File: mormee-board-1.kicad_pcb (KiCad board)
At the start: 4 copper layers, 40 x 60 mm, 167 parts, among them J2 24FLZ-SM2-TB, J3 USB4105-GF-A, J4 S2B-PH-SM4-TB(LF)(SN), J5 DM3BT-DSF-PEJS, M1 IMP34DT05TR, M2 IMP34DT05TR, Q1 AO3401A, SW1 EVQ-PUB02K, SW2 EVQ-PUB02K, U1 W25Q128JVSIQ, U10 MAX17048G+T10, U11 MP2637GR-P, U2 RTL8735BDM-A20-N04, U3 FDS9926A, U4 FT232RNL-REEL, U5 RT8097AHGE, U6 RT8097AHGE, U7 RT9080-28GJ5, U8 RT9080-18GJ5, U9 RT9080-12GJ5

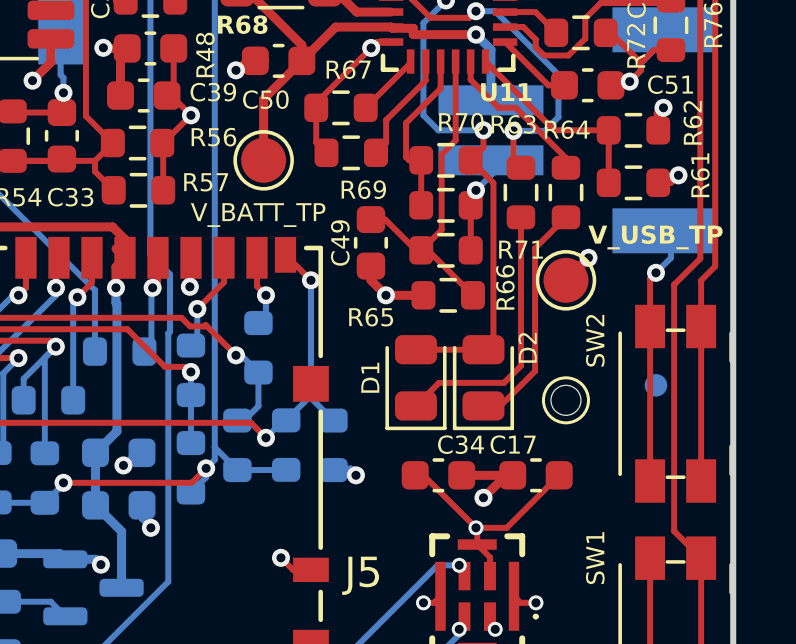
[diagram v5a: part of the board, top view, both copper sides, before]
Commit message: Updated LED footprint to 0603, which was easier to find
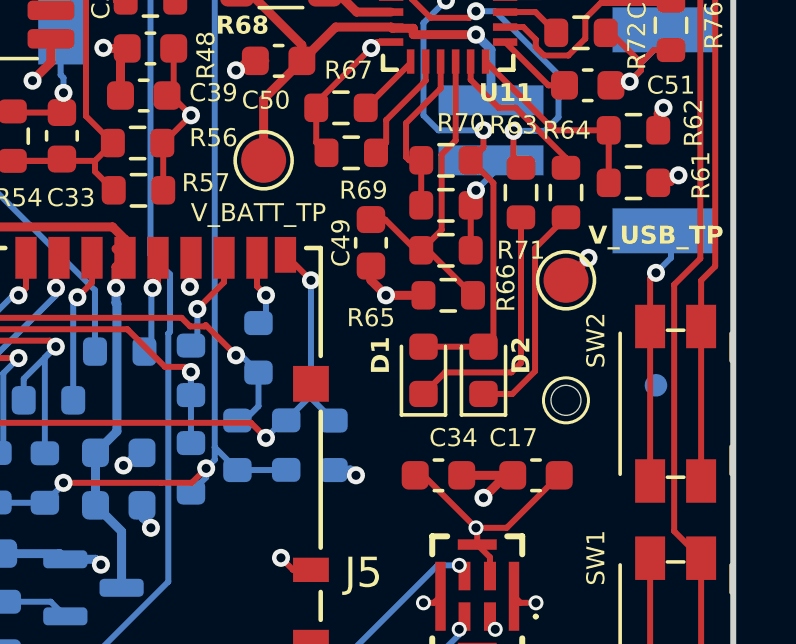
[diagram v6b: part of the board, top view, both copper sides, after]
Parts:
- C51, C53: value 100nF_10V -> 0.1uF_10V
- D1: value LED_2012_RED -> RED LED; footprint LED_SMD:LED_0805_2012Metric -> LED_SMD:LED_0603_1608Metric
- D2: value LED_2012_BLUE -> BLUE LED; footprint LED_SMD:LED_0805_2012Metric -> LED_SMD:LED_0603_1608Metric
- moved D1 0.35 mm to (99.0, 88.0)
- moved D2 0.25 mm to (101.0, 88.0)
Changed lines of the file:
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@@
 		)
 	)
-	(footprint "LED_SMD:LED_0805_2012Metric"
+	(footprint "LED_SMD:LED_0603_1608Metric"
 		(layer "F.Cu")
-		(at 101 88.25 90)
-		(descr "LED SMD 0805 (2012 Metric), square (rectangular) end terminal, IPC-7351 nominal, (Body size source: https://docs.google.com/spreadsheets/d/1BsfQQcO9C6DZCsRaXUlFlo91Tg2WpOkGARC1WS5S8t0/edit?usp=sharing), generated with kicad-footprint-generator")
+		(at 101 88 90)
+		(descr "LED SMD 0603 (1608 Metric), square (rectangular) end terminal, IPC-7351 nominal, (Body size source: http://www.tortai-tech.com/upload/download/2011102023233369053.pdf), generated with kicad-footprint-generator")
 		(tags "LED")
 		(property "Reference" "D2"
-			(at 1 1.5 90)
+			(at 0.5 1.25 90)
 			(layer "F.SilkS")
 			(effects
@@
 					(size 0.6 0.6)
 					(thickness 0.1)
+					(bold yes)
 				)
 			)
 		)
-		(property "Value" "LED_2012_BLUE"
-			(at 0 1.65 90)
+		(property "Value" "BLUE LED"
+			(at 0 1.43 90)
 			(layer "F.Fab")
 			(effects
@@
 		(attr smd)
 		(fp_line
-			(start 1 -0.96)
-			(end -1.685 -0.96)
+			(start 0.8 -0.735)
+			(end -1.485 -0.735)
 			(stroke
 				(width 0.12)
@@
 		)
 		(fp_line
-			(start -1.685 -0.96)
-			(end -1.685 0.96)
+			(start -1.485 -0.735)
+			(end -1.485 0.735)
 			(stroke
 				(width 0.12)
@@
 		)
 		(fp_line
-			(start -1.685 0.96)
-			(end 1 0.96)
+			(start -1.485 0.735)
+			(end 0.8 0.735)
 			(stroke
 				(width 0.12)
@@
 		)
 		(fp_rect
-			(start -1.68 -0.95)
-			(end 1.68 0.95)
+			(start -1.48 -0.73)
+			(end 1.48 0.73)
 			(stroke
 				(width 0.05)
@@
 		)
 		(fp_line
-			(start 1 -0.6)
-			(end -0.7 -0.6)
+			(start 0.8 -0.4)
+			(end -0.5 -0.4)
 			(stroke
 				(width 0.1)
@@
 		)
 		(fp_line
-			(start -0.7 -0.6)
-			(end -1 -0.3)
+			(start -0.5 -0.4)
+			(end -0.8 -0.1)
 			(stroke
 				(width 0.1)
@@
 		)
 		(fp_line
-			(start -1 -0.3)
-			(end -1 0.6)
+			(start -0.8 -0.1)
+			(end -0.8 0.4)
 			(stroke
 				(width 0.1)
@@
 		)
 		(fp_line
-			(start 1 0.6)
-			(end 1 -0.6)
+			(start 0.8 0.4)
+			(end 0.8 -0.4)
 			(stroke
 				(width 0.1)
@@
 		)
 		(fp_line
-			(start -1 0.6)
-			(end 1 0.6)
+			(start -0.8 0.4)
+			(end 0.8 0.4)
 			(stroke
 				(width 0.1)
@@
 		)
 		(fp_text user "${REFERENCE}"
-			(at 2.4375 0 90)
+			(at 0 0 90)
 			(layer "F.Fab")
 			(effects
 				(font
-					(size 0.6 0.6)
-					(thickness 0.1)
+					(size 0.4 0.4)
+					(thickness 0.06)
 				)
 			)
 		)
 		(pad "1" smd roundrect
-			(at -0.9375 0 90)
-			(size 0.975 1.4)
+			(at -0.7875 0 90)
+			(size 0.875 0.95)
 			(layers "F.Cu" "F.Mask" "F.Paste")
 			(roundrect_rratio 0.25)
@@
 		)
 		(pad "2" smd roundrect
-			(at 0.9375 0 90)
-			(size 0.975 1.4)
+			(at 0.7875 0 90)
+			(size 0.875 0.95)
 			(layers "F.Cu" "F.Mask" "F.Paste")
 			(roundrect_rratio 0.25)
@@
 		)
 		(embedded_fonts no)
-		(model "${KICAD9_3DMODEL_DIR}/LED_SMD.3dshapes/LED_0805_2012Metric.step"
+		(model "${KICAD9_3DMODEL_DIR}/LED_SMD.3dshapes/LED_0603_1608Metric.step"
 			(offset
 				(xyz 0 0 0)
@@
 			)
 		)
-		(property "Value" "100nF_10V"
+		(property "Value" "0.1uF_10V"
 			(at 0 1.43 0)
 			(layer "F.Fab")
@@
 		)
 	)
-	(footprint "LED_SMD:LED_0805_2012Metric"
+	(footprint "LED_SMD:LED_0603_1608Metric"
 		(layer "F.Cu")
-		(at 98.75 88.25 90)
-		(descr "LED SMD 0805 (2012 Metric), square (rectangular) end terminal, IPC-7351 nominal, (Body size source: https://docs.google.com/spreadsheets/d/1BsfQQcO9C6DZCsRaXUlFlo91Tg2WpOkGARC1WS5S8t0/edit?usp=sharing), generated with kicad-footprint-generator")
+		(at 99 88 90)
+		(descr "LED SMD 0603 (1608 Metric), square (rectangular) end terminal, IPC-7351 nominal, (Body size source: http://www.tortai-tech.com/upload/download/2011102023233369053.pdf), generated with kicad-footprint-generator")
 		(tags "LED")
 		(property "Reference" "D1"
-			(at 0 -1.5 90)
+			(at 0.5 -1.43 90)
 			(layer "F.SilkS")
 			(effects
@@
 					(size 0.6 0.6)
 					(thickness 0.1)
+					(bold yes)
 				)
 			)
 		)
-		(property "Value" "LED_2012_RED"
-			(at 0 1.65 90)
+		(property "Value" "RED LED"
+			(at 0 1.43 90)
 			(layer "F.Fab")
 			(effects
@@
 		(attr smd)
 		(fp_line
-			(start 1 -0.96)
-			(end -1.685 -0.96)
+			(start 0.8 -0.735)
+			(end -1.485 -0.735)
 			(stroke
 				(width 0.12)
@@
 		)
 		(fp_line
-			(start -1.685 -0.96)
-			(end -1.685 0.96)
+			(start -1.485 -0.735)
+			(end -1.485 0.735)
 			(stroke
 				(width 0.12)
@@
 		)
 		(fp_line
-			(start -1.685 0.96)
-			(end 1 0.96)
+			(start -1.485 0.735)
+			(end 0.8 0.735)
 			(stroke
 				(width 0.12)
@@
 		)
 		(fp_rect
-			(start -1.68 -0.95)
-			(end 1.68 0.95)
+			(start -1.48 -0.73)
+			(end 1.48 0.73)
 			(stroke
 				(width 0.05)
@@
 		)
 		(fp_line
-			(start 1 -0.6)
-			(end -0.7 -0.6)
+			(start 0.8 -0.4)
+			(end -0.5 -0.4)
 			(stroke
 				(width 0.1)
@@
 		)
 		(fp_line
-			(start -0.7 -0.6)
-			(end -1 -0.3)
+			(start -0.5 -0.4)
+			(end -0.8 -0.1)
 			(stroke
 				(width 0.1)
@@
 		)
 		(fp_line
-			(start -1 -0.3)
-			(end -1 0.6)
+			(start -0.8 -0.1)
+			(end -0.8 0.4)
 			(stroke
 				(width 0.1)
@@
 		)
 		(fp_line
-			(start 1 0.6)
-			(end 1 -0.6)
+			(start 0.8 0.4)
+			(end 0.8 -0.4)
 			(stroke
 				(width 0.1)
@@
 		)
 		(fp_line
-			(start -1 0.6)
-			(end 1 0.6)
+			(start -0.8 0.4)
+			(end 0.8 0.4)
 			(stroke
 				(width 0.1)
@@
 		)
 		(fp_text user "${REFERENCE}"
-			(at 2.6775 0.105 90)
+			(at 0 0 90)
 			(layer "F.Fab")
 			(effects
 				(font
-					(size 0.6 0.6)
-					(thickness 0.1)
+					(size 0.4 0.4)
+					(thickness 0.06)
 				)
 			)
 		)
 		(pad "1" smd roundrect
-			(at -0.9375 0 90)
-			(size 0.975 1.4)
+			(at -0.7875 0 90)
+			(size 0.875 0.95)
 			(layers "F.Cu" "F.Mask" "F.Paste")
 			(roundrect_rratio 0.25)
@@
 		)
 		(pad "2" smd roundrect
-			(at 0.9375 0 90)
-			(size 0.975 1.4)
+			(at 0.7875 0 90)
+			(size 0.875 0.95)
 			(layers "F.Cu" "F.Mask" "F.Paste")
 			(roundrect_rratio 0.25)
@@
 		)
 		(embedded_fonts no)
-		(model "${KICAD9_3DMODEL_DIR}/LED_SMD.3dshapes/LED_0805_2012Metric.step"
+		(model "${KICAD9_3DMODEL_DIR}/LED_SMD.3dshapes/LED_0603_1608Metric.step"
 			(offset
 				(xyz 0 0 0)
@@
 		(tags "resistor")
 		(property "Reference" "R63"
-			(at 2.25 -0.25 -0)
+			(at 2.25 -0.25 0)
 			(layer "F.SilkS")
 			(effects
@@
 			)
 		)
-		(property "Value" "100nF_10V"
+		(property "Value" "0.1uF_10V"
 			(at 0 1.43 0)
 			(layer "F.Fab")
@@
 		(tags "capacitor")
 		(property "Reference" "C17"
-			(at 0.75 1 0)
+			(at 0.75 1.25 0)
 			(layer "F.SilkS")
 			(effects
@@
 		(tags "capacitor")
 		(property "Reference" "C34"
-			(at -0.75 1 0)
+			(at -0.5 1.25 0)
 			(layer "F.SilkS")
 			(effects
@@
 	)
 	(segment
-		(start 101 87.3125)
-		(end 98.75 87.3125)
-		(width 0.2)
-		(layer "F.Cu")
-		(net 27)
-	)
-	(segment
 		(start 105.075 72.182835)
 		(end 104.445448 71.553283)
@@
 	)
 	(segment
-		(start 101.331 81.756)
-		(end 101.331 86.9815)
+		(start 101.307794 75.557794)
+		(end 101.199003 75.449003)
 		(width 0.2)
 		(layer "F.Cu")
@@
 	)
 	(segment
-		(start 101.307794 75.557794)
-		(end 101.199003 75.449003)
+		(start 101.331 81.756)
+		(end 101.331 86.8815)
 		(width 0.2)
 		(layer "F.Cu")
@@
 	)
 	(segment
-		(start 101.331 86.9815)
-		(end 101 87.3125)
+		(start 101.331 86.8815)
+		(end 101 87.2125)
+		(width 0.2)
+		(layer "F.Cu")
+		(net 27)
+	)
+	(segment
+		(start 101 87.2125)
+		(end 99 87.2125)
 		(width 0.2)
 		(layer "F.Cu")
@@
 	(segment
 		(start 102.25 82.9)
-		(end 102.25 87.849362)
+		(end 102.25 87.75)
 		(width 0.2)
 		(layer "F.Cu")
@@
 	)
 	(segment
-		(start 101.680362 88.419)
-		(end 99.5185 88.419)
+		(start 102.25 87.75)
+		(end 101.931 88.069)
 		(width 0.2)
 		(layer "F.Cu")
@@
 	)
 	(segment
-		(start 102.25 87.849362)
-		(end 101.680362 88.419)
+		(start 99.7185 88.069)
+		(end 99 88.7875)
 		(width 0.2)
 		(layer "F.Cu")
@@
 	)
 	(segment
-		(start 99.5185 88.419)
-		(end 98.75 89.1875)
+		(start 101.931 88.069)
+		(end 99.7185 88.069)
 		(width 0.2)
 		(layer "F.Cu")
@@
 	)
 	(segment
-		(start 101.5625 89.1875)
-		(end 101 89.1875)
+		(start 101.9625 88.7875)
+		(end 101 88.7875)
 		(width 0.2)
 		(layer "F.Cu")
@@
 	)
 	(segment
-		(start 103.75 82.9)
-		(end 102.719 83.931)
+		(start 102.719 88.031)
+		(end 101.9625 88.7875)
 		(width 0.2)
 		(layer "F.Cu")
@@
 	)
 	(segment
-		(start 102.719 88.031)
-		(end 101.5625 89.1875)
+		(start 103.75 82.9)
+		(end 102.719 83.931)
 		(width 0.2)
 		(layer "F.Cu")

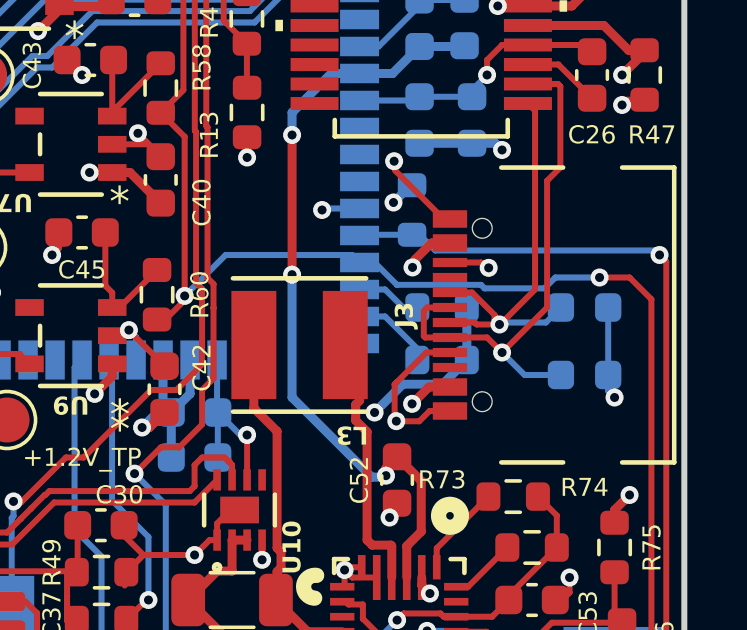
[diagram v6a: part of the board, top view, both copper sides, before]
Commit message: Updated USB connector pads to be manufacturable
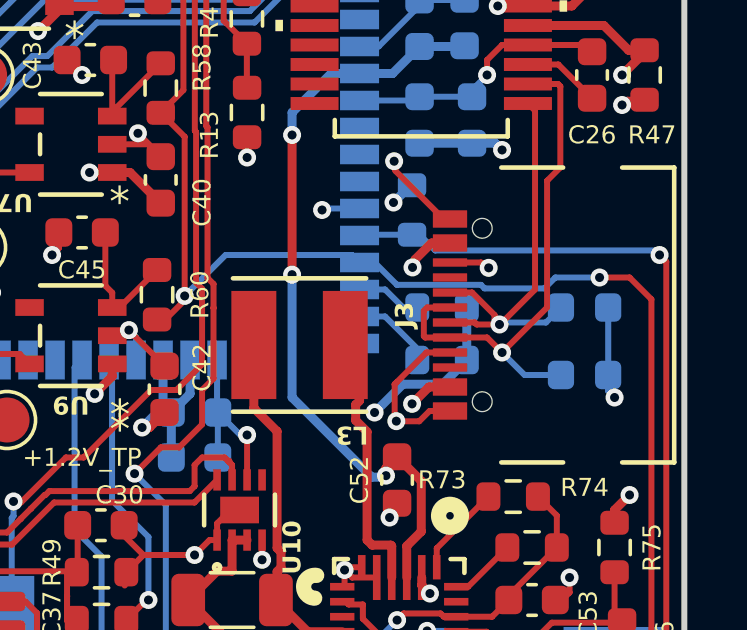
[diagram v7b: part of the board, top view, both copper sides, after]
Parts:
- R55: value 44.RES_0603_1%_2K -> 2K_1%
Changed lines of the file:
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@@
 		(pad "A1-B12" smd rect
 			(at -3.2 -3.4858 90)
-			(size 0.5842 1.143)
+			(size 0.58 1.143)
 			(layers "F.Cu" "F.Mask" "F.Paste")
 			(net 1 "GND")
@@
 		(pad "A4-B9" smd rect
 			(at -2.400001 -3.4858 90)
-			(size 0.5842 1.143)
+			(size 0.58 1.143)
 			(layers "F.Cu" "F.Mask" "F.Paste")
 			(net 14 "V_USB")
@@
 		(pad "A5" smd rect
 			(at -1.25 -3.4858 90)
-			(size 0.3048 1.143)
+			(size 0.28 1.143)
 			(layers "F.Cu" "F.Mask" "F.Paste")
 			(net 1 "GND")
@@
 		(pad "A6" smd rect
 			(at -0.25 -3.4858 90)
-			(size 0.3048 1.143)
+			(size 0.28 1.143)
 			(layers "F.Cu" "F.Mask" "F.Paste")
 			(net 44 "/Debug Interface/USB_P")
@@
 		(pad "A7" smd rect
 			(at 0.25 -3.4858 90)
-			(size 0.3048 1.143)
+			(size 0.28 1.143)
 			(layers "F.Cu" "F.Mask" "F.Paste")
 			(net 42 "/Debug Interface/USB_N")
@@
 		(pad "A8" smd rect
 			(at 1.25 -3.4858 90)
-			(size 0.3048 1.143)
+			(size 0.28 1.143)
 			(layers "F.Cu" "F.Mask" "F.Paste")
 			(net 43 "unconnected-(J3-SBU1-PadA8)")
@@
 		(pad "B1-A12" smd rect
 			(at 3.2 -3.4858 90)
-			(size 0.5842 1.143)
+			(size 0.58 1.143)
 			(layers "F.Cu" "F.Mask" "F.Paste")
 			(net 1 "GND")
@@
 		(pad "B4-A9" smd rect
 			(at 2.400001 -3.4858 90)
-			(size 0.5842 1.143)
+			(size 0.58 1.143)
 			(layers "F.Cu" "F.Mask" "F.Paste")
 			(net 14 "V_USB")
@@
 		(pad "B5" smd rect
 			(at 1.749999 -3.4858 90)
-			(size 0.3048 1.143)
+			(size 0.28 1.143)
 			(layers "F.Cu" "F.Mask" "F.Paste")
 			(net 1 "GND")
@@
 		(pad "B6" smd rect
 			(at 0.750001 -3.4858 90)
-			(size 0.3048 1.143)
+			(size 0.28 1.143)
 			(layers "F.Cu" "F.Mask" "F.Paste")
 			(net 44 "/Debug Interface/USB_P")
@@
 		(pad "B7" smd rect
 			(at -0.750001 -3.4858 90)
-			(size 0.3048 1.143)
+			(size 0.28 1.143)
 			(layers "F.Cu" "F.Mask" "F.Paste")
 			(net 42 "/Debug Interface/USB_N")
@@
 		(pad "B8" smd rect
 			(at -1.749999 -3.4858 90)
-			(size 0.3048 1.143)
+			(size 0.28 1.143)
 			(layers "F.Cu" "F.Mask" "F.Paste")
 			(net 45 "unconnected-(J3-SBU2-PadB8)")
@@
 			)
 		)
-		(property "Value" "44.RES_0603_1%_2K"
+		(property "Value" "2K_1%"
 			(at 0 1.43 90)
 			(layer "F.Fab")
